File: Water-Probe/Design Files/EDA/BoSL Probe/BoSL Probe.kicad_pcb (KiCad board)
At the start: 2 copper layers, 29 x 18 mm, 9 parts, among them J1 8P8C_Shielded, J2 KeyStone_Screw_Small, J3 KeyStone_Screw_Small, U1 MS5803-01BA, U2 DS18B20

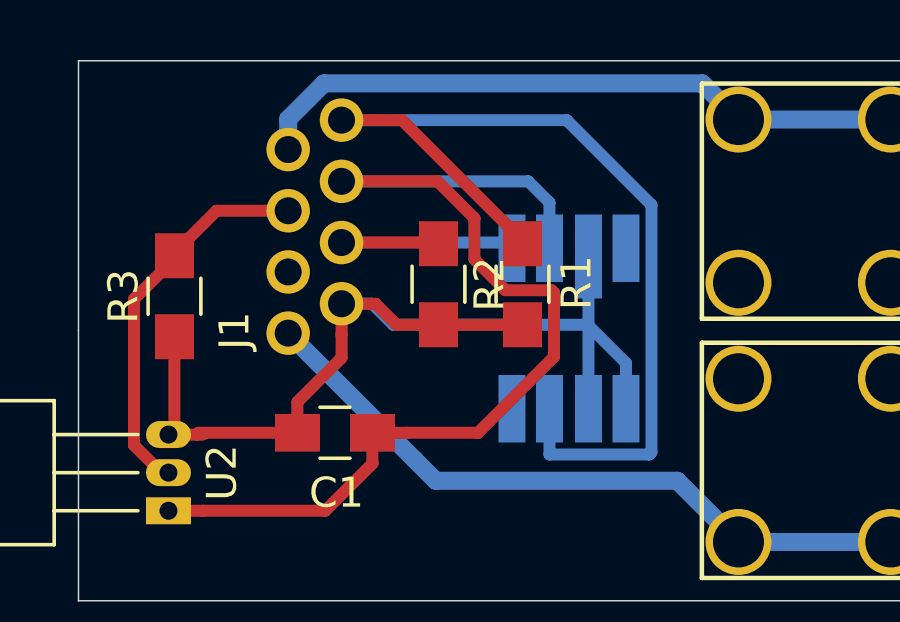
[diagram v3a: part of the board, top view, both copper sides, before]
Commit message: added rendering of probe
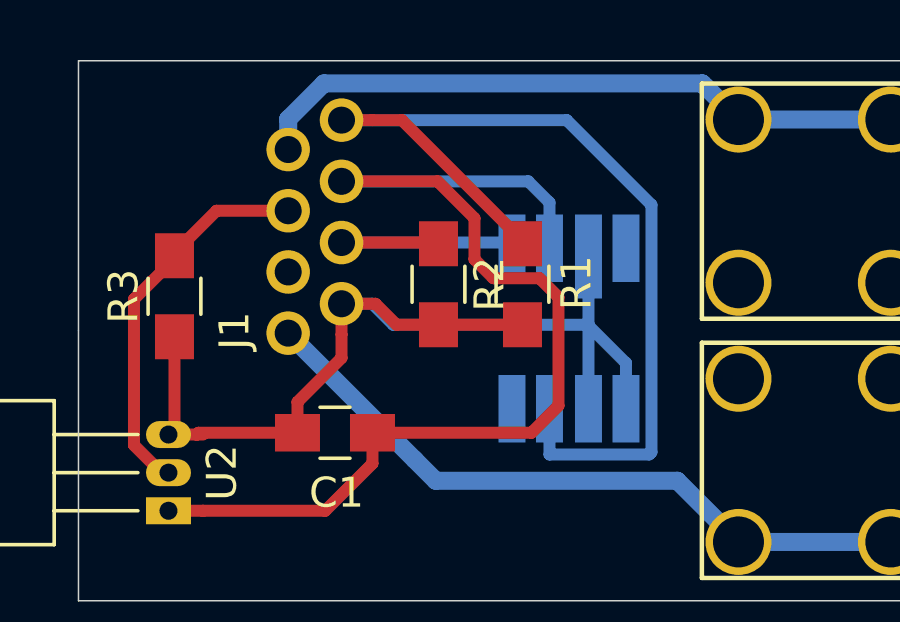
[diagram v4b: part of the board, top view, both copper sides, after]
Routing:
- net Green: track 35.9 -> 37.1 mm
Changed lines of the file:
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@@
     (thickness 1.6)
     (drawings 5)
-    (tracks 72)
+    (tracks 71)
     (zones 0)
     (modules 9)
@@
   )
   (setup
-    (last_trace_width 0.6)
+    (last_trace_width 0.4)
     (user_trace_width 0.4)
     (user_trace_width 0.6)
@@
     (mod_text_size 1 1)
     (mod_text_width 0.15)
-    (pad_size 1.524 1.524)
-    (pad_drill 0.762)
+    (pad_size 2.2 2.2)
+    (pad_drill 1.7)
     (pad_to_mask_clearance 0.051)
     (solder_mask_min_width 0.25)
@@
     (pad 1 thru_hole circle (at 2.72 -5 270) (size 2.2 2.2) (drill 1.7) (layers *.Cu *.Mask)
       (net 3 A0))
-    (pad 1 thru_hole circle (at -2.72 0.08) (size 2.2 2.2) (drill 1.7) (layers *.Cu *.Mask)
-      (net 3 A0))
-    (pad 1 thru_hole circle (at -2.72 -5 270) (size 2.2 2.2) (drill 1.7) (layers *.Cu *.Mask)
-      (net 3 A0))
+    (pad 1 thru_hole circle (at -2.72 0.08) (size 2.2 2.2) (drill 1.7) (layers *.Cu *.Mask))
+    (pad 1 thru_hole circle (at -2.72 -5 270) (size 2.2 2.2) (drill 1.7) (layers *.Cu *.Mask))
     (model "D:/data/My Documents/Monash/Monash-BoSL/Water-Probe/Design Files/CAD/Parts/Keystone_Screw_Small.wrl"
       (at (xyz 0 0 0))
@@
     (pad 1 thru_hole circle (at -2.72 0.08) (size 2.2 2.2) (drill 1.7) (layers *.Cu *.Mask)
       (net 4 A3))
-    (pad 1 thru_hole circle (at 2.72 -5 270) (size 2.2 2.2) (drill 1.7) (layers *.Cu *.Mask)
-      (net 4 A3))
-    (pad 1 thru_hole circle (at 2.72 0.08) (size 2.2 2.2) (drill 1.7) (layers *.Cu *.Mask)
-      (net 4 A3))
+    (pad 1 thru_hole circle (at 2.72 -5 270) (size 2.2 2.2) (drill 1.7) (layers *.Cu *.Mask))
+    (pad 1 thru_hole circle (at 2.72 0.08) (size 2.2 2.2) (drill 1.7) (layers *.Cu *.Mask))
     (model "D:/data/My Documents/Monash/Monash-BoSL/Water-Probe/Design Files/CAD/Parts/Keystone_Screw_Small.wrl"
       (at (xyz 0 0 0))
@@
   (segment (start 109.8 104.425) (end 108.225 106) (width 0.4) (layer F.Cu) (net 1))
   (segment (start 109.8 103.4) (end 109.8 104.425) (width 0.4) (layer F.Cu) (net 1) (status 10))
-  (segment (start 111.971458 95.02) (end 113.2 96.248542) (width 0.4) (layer F.Cu) (net 1))
-  (segment (start 108.768 95.02) (end 111.971458 95.02) (width 0.4) (layer F.Cu) (net 1) (status 10))
-  (segment (start 110.95 103.4) (end 109.8 103.4) (width 0.4) (layer F.Cu) (net 1) (status 20))
-  (segment (start 113.320002 103.4) (end 110.95 103.4) (width 0.4) (layer F.Cu) (net 1))
-  (segment (start 115.850001 100.870001) (end 113.320002 103.4) (width 0.4) (layer F.Cu) (net 1))
-  (segment (start 115.850001 98.729999) (end 115.850001 100.870001) (width 0.4) (layer F.Cu) (net 1))
-  (segment (start 115.770001 98.649999) (end 115.850001 98.729999) (width 0.4) (layer F.Cu) (net 1))
-  (segment (start 114.229997 98.649999) (end 115.770001 98.649999) (width 0.4) (layer F.Cu) (net 1))
-  (segment (start 113.2 97.620002) (end 114.229997 98.649999) (width 0.4) (layer F.Cu) (net 1))
-  (segment (start 113.2 96.248542) (end 113.2 97.620002) (width 0.4) (layer F.Cu) (net 1))
+  (segment (start 113.2 96.248542) (end 111.971458 95.02) (width 0.4) (layer F.Cu) (net 1))
+  (segment (start 111.971458 95.02) (end 108.768 95.02) (width 0.4) (layer F.Cu) (net 1))
+  (segment (start 113.2 97.620002) (end 113.2 96.248542) (width 0.4) (layer F.Cu) (net 1))
+  (segment (start 116 102.5) (end 116 98.879998) (width 0.4) (layer F.Cu) (net 1))
+  (segment (start 109.8 103.4) (end 115.1 103.4) (width 0.4) (layer F.Cu) (net 1))
+  (segment (start 116 98.879998) (end 115.370003 98.250001) (width 0.4) (layer F.Cu) (net 1))
+  (segment (start 115.1 103.4) (end 116 102.5) (width 0.4) (layer F.Cu) (net 1))
+  (segment (start 115.370003 98.250001) (end 113.829999 98.250001) (width 0.4) (layer F.Cu) (net 1))
+  (segment (start 113.829999 98.250001) (end 113.2 97.620002) (width 0.4) (layer F.Cu) (net 1))
   (segment (start 117 99.825) (end 117 99.8) (width 0.4) (layer B.Cu) (net 2))
   (segment (start 118.25 101.075) (end 117 99.825) (width 0.4) (layer B.Cu) (net 2))

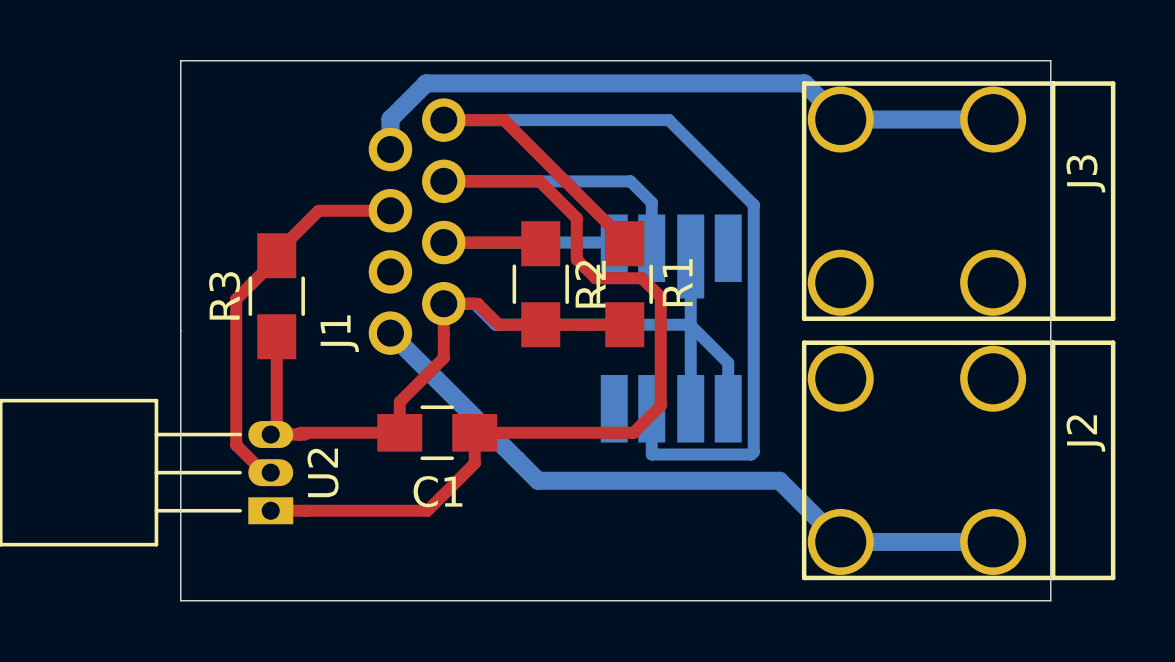
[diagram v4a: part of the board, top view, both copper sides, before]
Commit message: adding rev 0.1 of sensor board pcb
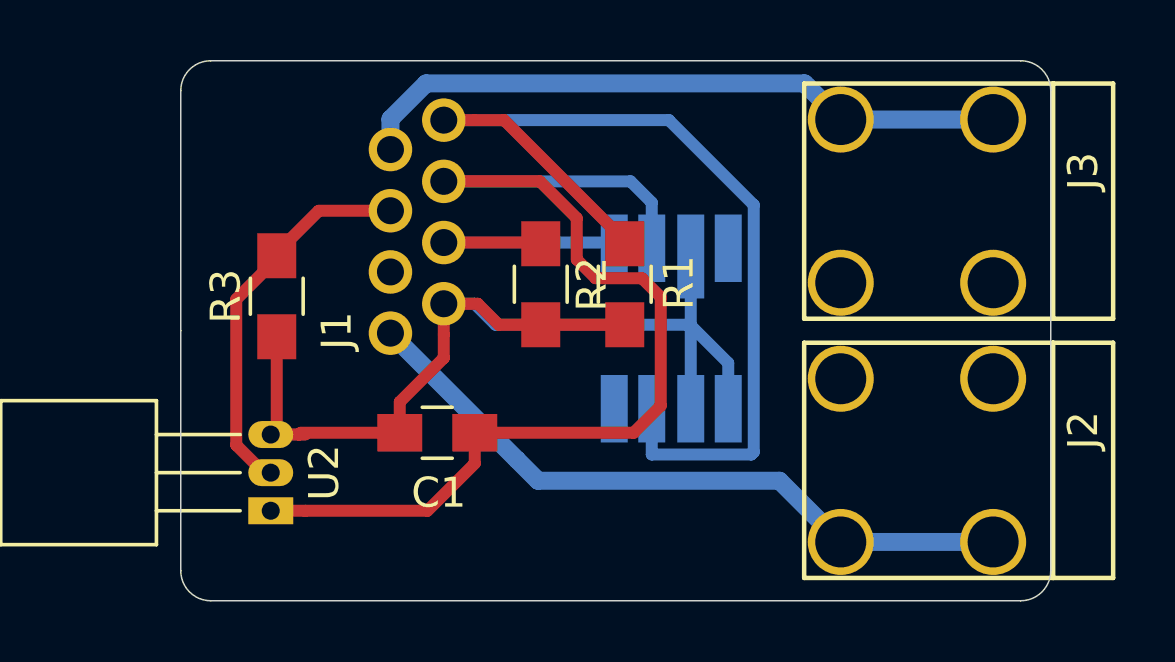
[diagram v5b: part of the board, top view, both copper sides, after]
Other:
- outline, holes or cut-outs redrawn
- board text added: "BoSL-Probe rev 0.1"
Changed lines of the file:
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@@
   (general
     (thickness 1.6)
-    (drawings 5)
+    (drawings 10)
     (tracks 71)
     (zones 0)
@@
   )
   (setup
-    (last_trace_width 0.4)
+    (last_trace_width 0.25)
     (user_trace_width 0.4)
     (user_trace_width 0.6)
@@
       (outputformat 1)
       (mirror false)
-      (drillshape 1)
+      (drillshape 0)
       (scaleselection 1)
-      (outputdirectory ""))
+      (outputdirectory "../../Production Files/Gerber/"))
   )
   (net 0 "")
@@
     )
   )
-  (gr_line (start 129 91) (end 129 109) (layer Edge.Cuts) (width 0.05))
-  (gr_line (start 100 109) (end 129 109) (layer Edge.Cuts) (width 0.05))
-  (gr_line (start 100 100) (end 100 109) (layer Edge.Cuts) (width 0.05))
-  (gr_line (start 100 91) (end 129 91) (layer Edge.Cuts) (width 0.05))
-  (gr_line (start 100 100) (end 100 91) (layer Edge.Cuts) (width 0.05))
+  (gr_text "BoSL-Probe\nrev 0.1" (at 114 107) (layer B.SilkS)
+    (effects (font (size 1 1) (thickness 0.15)) (justify mirror))
+  )
+  (gr_arc (start 128 92) (end 129 92) (angle -90) (layer Edge.Cuts) (width 0.05))
+  (gr_arc (start 128 108) (end 128 109) (angle -90) (layer Edge.Cuts) (width 0.05))
+  (gr_arc (start 101 108) (end 100 108) (angle -90) (layer Edge.Cuts) (width 0.05))
+  (gr_arc (start 101 92) (end 101 91) (angle -90) (layer Edge.Cuts) (width 0.05))
+  (gr_line (start 129 92) (end 129 108) (layer Edge.Cuts) (width 0.05))
+  (gr_line (start 101 109) (end 128 109) (layer Edge.Cuts) (width 0.05))
+  (gr_line (start 100 100) (end 100 108) (layer Edge.Cuts) (width 0.05))
+  (gr_line (start 101 91) (end 128 91) (layer Edge.Cuts) (width 0.05))
+  (gr_line (start 100 100) (end 100 92) (layer Edge.Cuts) (width 0.05))
   (segment (start 115.7 95.725) (end 115.7 97.25) (width 0.4) (layer B.Cu) (net 1) (status 20))
   (segment (start 114.995 95.02) (end 115.7 95.725) (width 0.4) (layer B.Cu) (net 1))

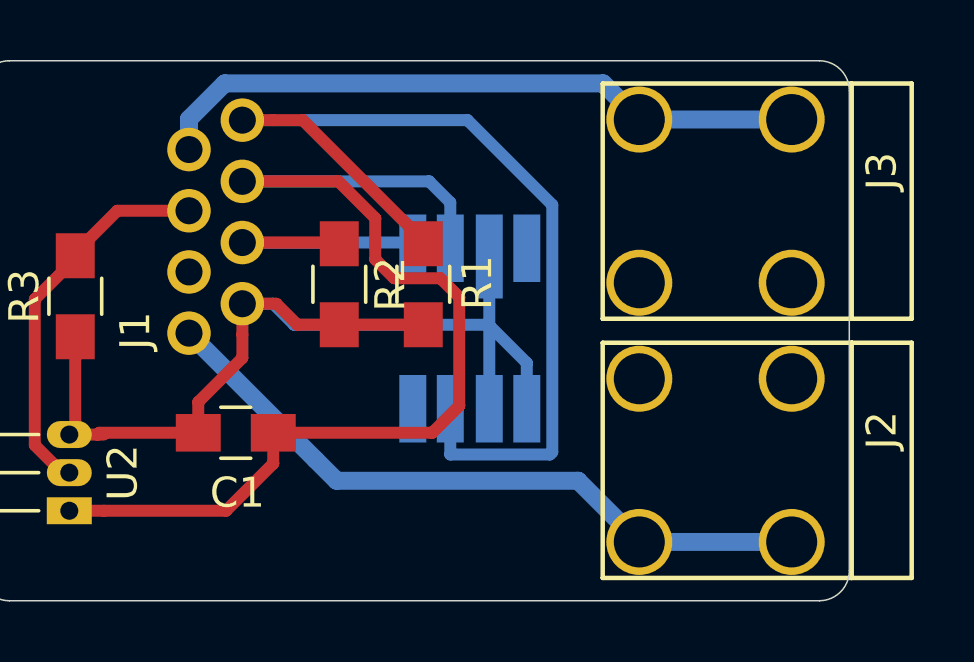
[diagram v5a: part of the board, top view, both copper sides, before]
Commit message: changed probe EC footprint to screw terminal cleaned up bosl GPS code
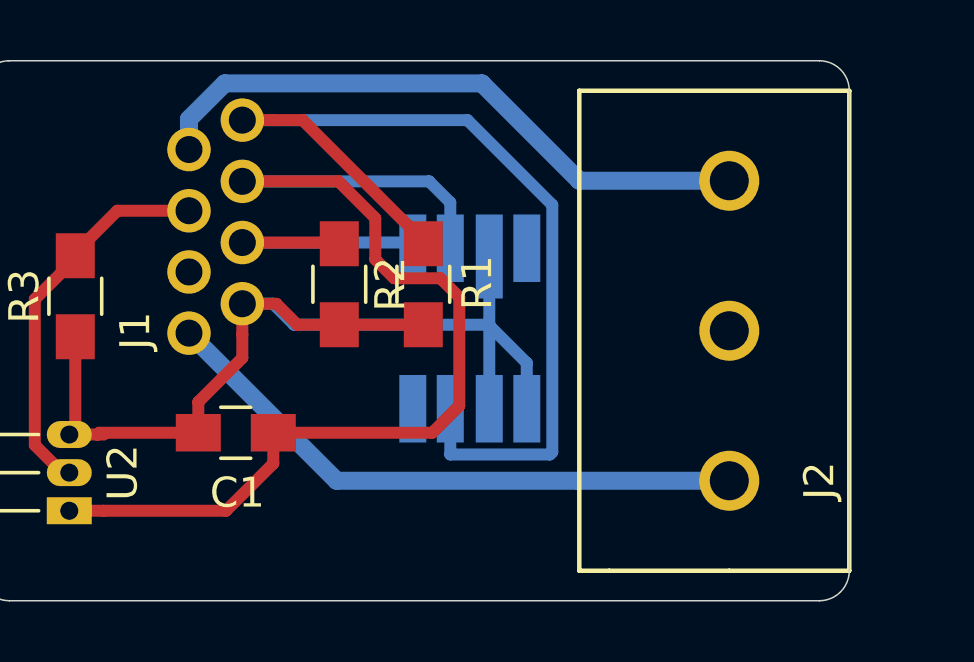
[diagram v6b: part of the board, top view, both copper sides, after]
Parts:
- removed J3: KeyStone_Screw_Small, Project:KeyStone_Screw_Small
- J2: value KeyStone_Screw_Small -> Screw_Terminal_01x03; footprint Project:KeyStone_Screw_Small -> Project:Screw_Terminals_1x3
- moved J2 3.00 mm to (125.0, 105.0), turned to 90 degrees
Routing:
- net A0: track 23.0 -> 20.0 mm
- net A3: track 22.1 -> 20.9 mm
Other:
- board text added: "BoSL-Probe rev 0.2"
- board text removed: "BoSL-Probe rev 0.1"
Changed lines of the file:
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@@
     (thickness 1.6)
     (drawings 10)
-    (tracks 71)
+    (tracks 68)
     (zones 0)
-    (modules 9)
+    (modules 8)
     (nets 8)
   )
@@
   )
   (setup
-    (last_trace_width 0.25)
+    (last_trace_width 0.6)
     (user_trace_width 0.4)
     (user_trace_width 0.6)
@@
     )
   )
-  (module Project:KeyStone_Screw_Small (layer F.Cu)
-    (at 122.08 104.32 270)
-    (fp_text reference J2 (at -1 -8 90) (layer F.SilkS)
-      (effects (font (size 1 1) (thickness 0.15)))
-    )
-    (fp_text value KeyStone_Screw_Small (at -1 -2 90) (layer F.Fab)
-      (effects (font (size 1 1) (thickness 0.15)))
-    )
-    (fp_line (start -3.92 -9) (end 3.92 -9) (layer F.SilkS) (width 0.15))
-    (fp_line (start -3.92 -7) (end 3.92 -7) (layer F.SilkS) (width 0.15))
-    (fp_line (start -3.92 1.3) (end 3.92 1.3) (layer F.SilkS) (width 0.15))
-    (fp_line (start -3.92 -7) (end -3.92 -9) (layer F.SilkS) (width 0.15))
-    (fp_line (start 3.92 -7) (end 3.92 -9) (layer F.SilkS) (width 0.15))
-    (fp_line (start -3.92 -7) (end -3.92 1.3) (layer F.SilkS) (width 0.15))
-    (fp_line (start 3.92 -7) (end 3.92 1.3) (layer F.SilkS) (width 0.15))
-    (pad 1 thru_hole circle (at 2.72 0.08) (size 2.2 2.2) (drill 1.7) (layers *.Cu *.Mask)
+  (module Project:Screw_Terminals_1x3 (layer F.Cu)
+    (at 125 105 90)
+    (fp_text reference J2 (at 0 3 90) (layer F.SilkS)
+      (effects (font (size 1 1) (thickness 0.15)))
+    )
+    (fp_text value Screw_Terminal_01x03 (at 5 -3 90) (layer F.Fab)
+      (effects (font (size 1 1) (thickness 0.15)))
+    )
+    (fp_line (start -3 -5) (end -3 -4) (layer F.SilkS) (width 0.15))
+    (fp_line (start 13 -5) (end -3 -5) (layer F.SilkS) (width 0.15))
+    (fp_line (start -3 0) (end -3 4) (layer F.SilkS) (width 0.15))
+    (fp_line (start -3 4) (end 13 4) (layer F.SilkS) (width 0.15))
+    (fp_line (start -3 -4) (end -3 0) (layer F.SilkS) (width 0.15))
+    (fp_line (start 13 -5) (end 13 4) (layer F.SilkS) (width 0.15))
+    (pad 3 thru_hole circle (at 10 0 90) (size 2 2) (drill 1.3) (layers *.Cu *.Mask)
+      (net 4 A3))
+    (pad 2 thru_hole circle (at 5 0 90) (size 2 2) (drill 1.3) (layers *.Cu *.Mask))
+    (pad 1 thru_hole circle (at 0 0 90) (size 2 2) (drill 1.3) (layers *.Cu *.Mask)
       (net 3 A0))
-    (pad 1 thru_hole circle (at 2.72 -5 270) (size 2.2 2.2) (drill 1.7) (layers *.Cu *.Mask)
-      (net 3 A0))
-    (pad 1 thru_hole circle (at -2.72 0.08) (size 2.2 2.2) (drill 1.7) (layers *.Cu *.Mask))
-    (pad 1 thru_hole circle (at -2.72 -5 270) (size 2.2 2.2) (drill 1.7) (layers *.Cu *.Mask))
-    (model "D:/data/My Documents/Monash/Monash-BoSL/Water-Probe/Design Files/CAD/Parts/Keystone_Screw_Small.wrl"
-      (at (xyz 0 0 0))
-      (scale (xyz 1 1 1))
-      (rotate (xyz 0 0 0))
-    )
-  )
-  (module Project:KeyStone_Screw_Small (layer F.Cu)
-    (at 122.08 95.68 270)
-    (fp_text reference J3 (at -1 -8 90) (layer F.SilkS)
-      (effects (font (size 1 1) (thickness 0.15)))
-    )
-    (fp_text value KeyStone_Screw_Small (at -1 -2 90) (layer F.Fab)
-      (effects (font (size 1 1) (thickness 0.15)))
-    )
-    (fp_line (start 3.92 -7) (end 3.92 1.3) (layer F.SilkS) (width 0.15))
-    (fp_line (start -3.92 -7) (end -3.92 1.3) (layer F.SilkS) (width 0.15))
-    (fp_line (start 3.92 -7) (end 3.92 -9) (layer F.SilkS) (width 0.15))
-    (fp_line (start -3.92 -7) (end -3.92 -9) (layer F.SilkS) (width 0.15))
-    (fp_line (start -3.92 1.3) (end 3.92 1.3) (layer F.SilkS) (width 0.15))
-    (fp_line (start -3.92 -7) (end 3.92 -7) (layer F.SilkS) (width 0.15))
-    (fp_line (start -3.92 -9) (end 3.92 -9) (layer F.SilkS) (width 0.15))
-    (pad 1 thru_hole circle (at -2.72 -5 270) (size 2.2 2.2) (drill 1.7) (layers *.Cu *.Mask)
-      (net 4 A3))
-    (pad 1 thru_hole circle (at -2.72 0.08) (size 2.2 2.2) (drill 1.7) (layers *.Cu *.Mask)
-      (net 4 A3))
-    (pad 1 thru_hole circle (at 2.72 -5 270) (size 2.2 2.2) (drill 1.7) (layers *.Cu *.Mask))
-    (pad 1 thru_hole circle (at 2.72 0.08) (size 2.2 2.2) (drill 1.7) (layers *.Cu *.Mask))
-    (model "D:/data/My Documents/Monash/Monash-BoSL/Water-Probe/Design Files/CAD/Parts/Keystone_Screw_Small.wrl"
-      (at (xyz 0 0 0))
-      (scale (xyz 1 1 1))
-      (rotate (xyz 0 0 0))
-    )
-  )
-  (gr_text "BoSL-Probe\nrev 0.1" (at 114 107) (layer B.SilkS)
+  )
+  (gr_text "BoSL-Probe\nrev 0.2" (at 114 107) (layer B.SilkS)
     (effects (font (size 1 1) (thickness 0.15)) (justify mirror))
   )
@@
   (segment (start 109.8 103.4) (end 109.8 104.425) (width 0.4) (layer F.Cu) (net 1) (status 10))
   (segment (start 113.2 96.248542) (end 111.971458 95.02) (width 0.4) (layer F.Cu) (net 1))
-  (segment (start 111.971458 95.02) (end 108.768 95.02) (width 0.4) (layer F.Cu) (net 1))
+  (segment (start 111.971458 95.02) (end 108.768 95.02) (width 0.4) (layer F.Cu) (net 1) (status 20))
   (segment (start 113.2 97.620002) (end 113.2 96.248542) (width 0.4) (layer F.Cu) (net 1))
   (segment (start 116 102.5) (end 116 98.879998) (width 0.4) (layer F.Cu) (net 1))
-  (segment (start 109.8 103.4) (end 115.1 103.4) (width 0.4) (layer F.Cu) (net 1))
+  (segment (start 109.8 103.4) (end 115.1 103.4) (width 0.4) (layer F.Cu) (net 1) (status 10))
   (segment (start 116 98.879998) (end 115.370003 98.250001) (width 0.4) (layer F.Cu) (net 1))
   (segment (start 115.1 103.4) (end 116 102.5) (width 0.4) (layer F.Cu) (net 1))
@@
   (segment (start 103.2 100.2) (end 103.2 103.26) (width 0.4) (layer F.Cu) (net 2) (status 30))
   (segment (start 114.8 99.8) (end 112 99.8) (width 0.4) (layer F.Cu) (net 2) (status 30))
-  (segment (start 111.205 104.295) (end 106.99 100.08) (width 0.6) (layer B.Cu) (net 3))
-  (segment (start 111.91 105) (end 111.205 104.295) (width 0.6) (layer B.Cu) (net 3))
-  (segment (start 122 107.04) (end 119.96 105) (width 0.6) (layer B.Cu) (net 3))
-  (segment (start 119.96 105) (end 111.91 105) (width 0.6) (layer B.Cu) (net 3))
-  (segment (start 122 107.04) (end 127.08 107.04) (width 0.6) (layer B.Cu) (net 3))
-  (segment (start 120.900001 91.860001) (end 122 92.96) (width 0.6) (layer B.Cu) (net 4))
-  (segment (start 120.794999 91.754999) (end 120.900001 91.860001) (width 0.6) (layer B.Cu) (net 4))
-  (segment (start 108.179999 91.754999) (end 120.794999 91.754999) (width 0.6) (layer B.Cu) (net 4))
+  (segment (start 119.96 105) (end 125 105) (width 0.6) (layer B.Cu) (net 3))
+  (segment (start 106.99 100.08) (end 111.91 105) (width 0.6) (layer B.Cu) (net 3))
+  (segment (start 111.91 105) (end 119.96 105) (width 0.6) (layer B.Cu) (net 3))
   (segment (start 106.99 92.944998) (end 108.179999 91.754999) (width 0.6) (layer B.Cu) (net 4))
-  (segment (start 106.99 93.96) (end 106.99 92.944998) (width 0.6) (layer B.Cu) (net 4))
-  (segment (start 122 92.96) (end 127.08 92.96) (width 0.6) (layer B.Cu) (net 4))
+  (segment (start 106.99 93.96) (end 106.99 92.944998) (width 0.6) (layer B.Cu) (net 4) (status 10))
+  (segment (start 108.179999 91.754999) (end 116.754999 91.754999) (width 0.6) (layer B.Cu) (net 4))
+  (segment (start 120 95) (end 125 95) (width 0.6) (layer B.Cu) (net 4))
+  (segment (start 116.754999 91.754999) (end 120 95) (width 0.6) (layer B.Cu) (net 4))
   (segment (start 114.26 97.06) (end 114.45 97.25) (width 0.4) (layer B.Cu) (net 5) (status 30))
   (segment (start 108.768 97.06) (end 114.26 97.06) (width 0.4) (layer B.Cu) (net 5) (status 30))
